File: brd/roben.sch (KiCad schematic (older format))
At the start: 92 parts, among them J1 POWER IN, J10 GND, J11 A, J12 C, J13 B, J14 D, J2 BT HC-05, J3 1+, J4 1-, J5 2+, J6 2-, J7 +V, J8 GND, J9 +V, Q1 BUK7Y98, Q2 BC856, SW1 POWER ON, SW2 SW_PUSH, SW3 SW_PUSH, U1 Ardunano, U2 LM3488, U3 SN754410N, U4 LM2902N

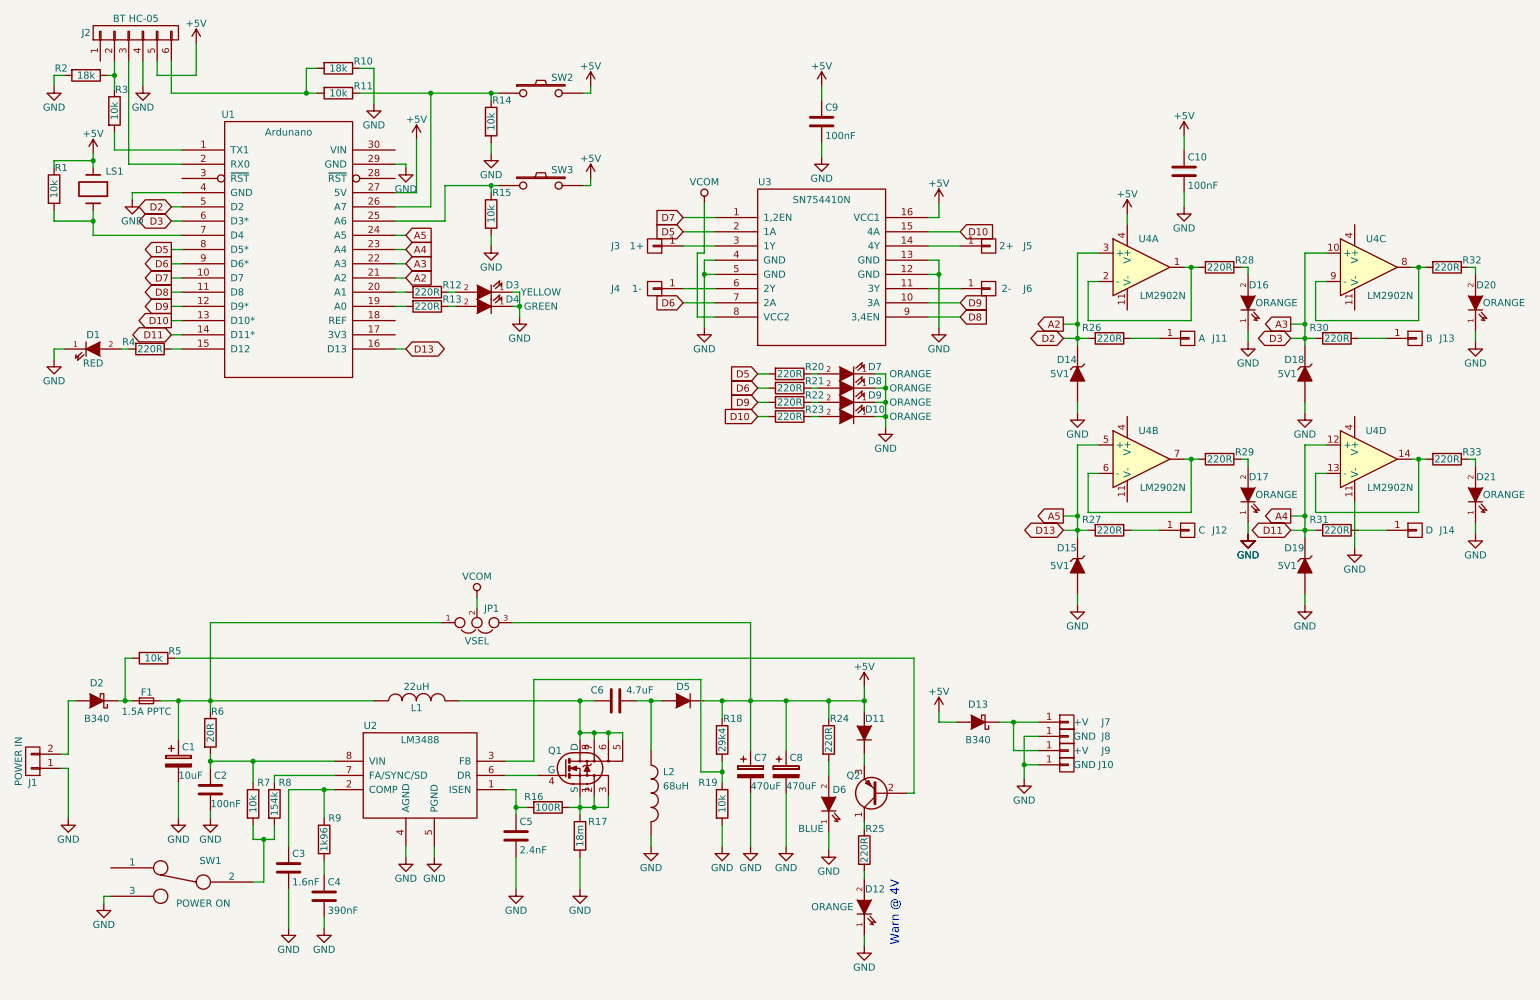
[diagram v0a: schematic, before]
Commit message: chg: creada netlist y asociaciones
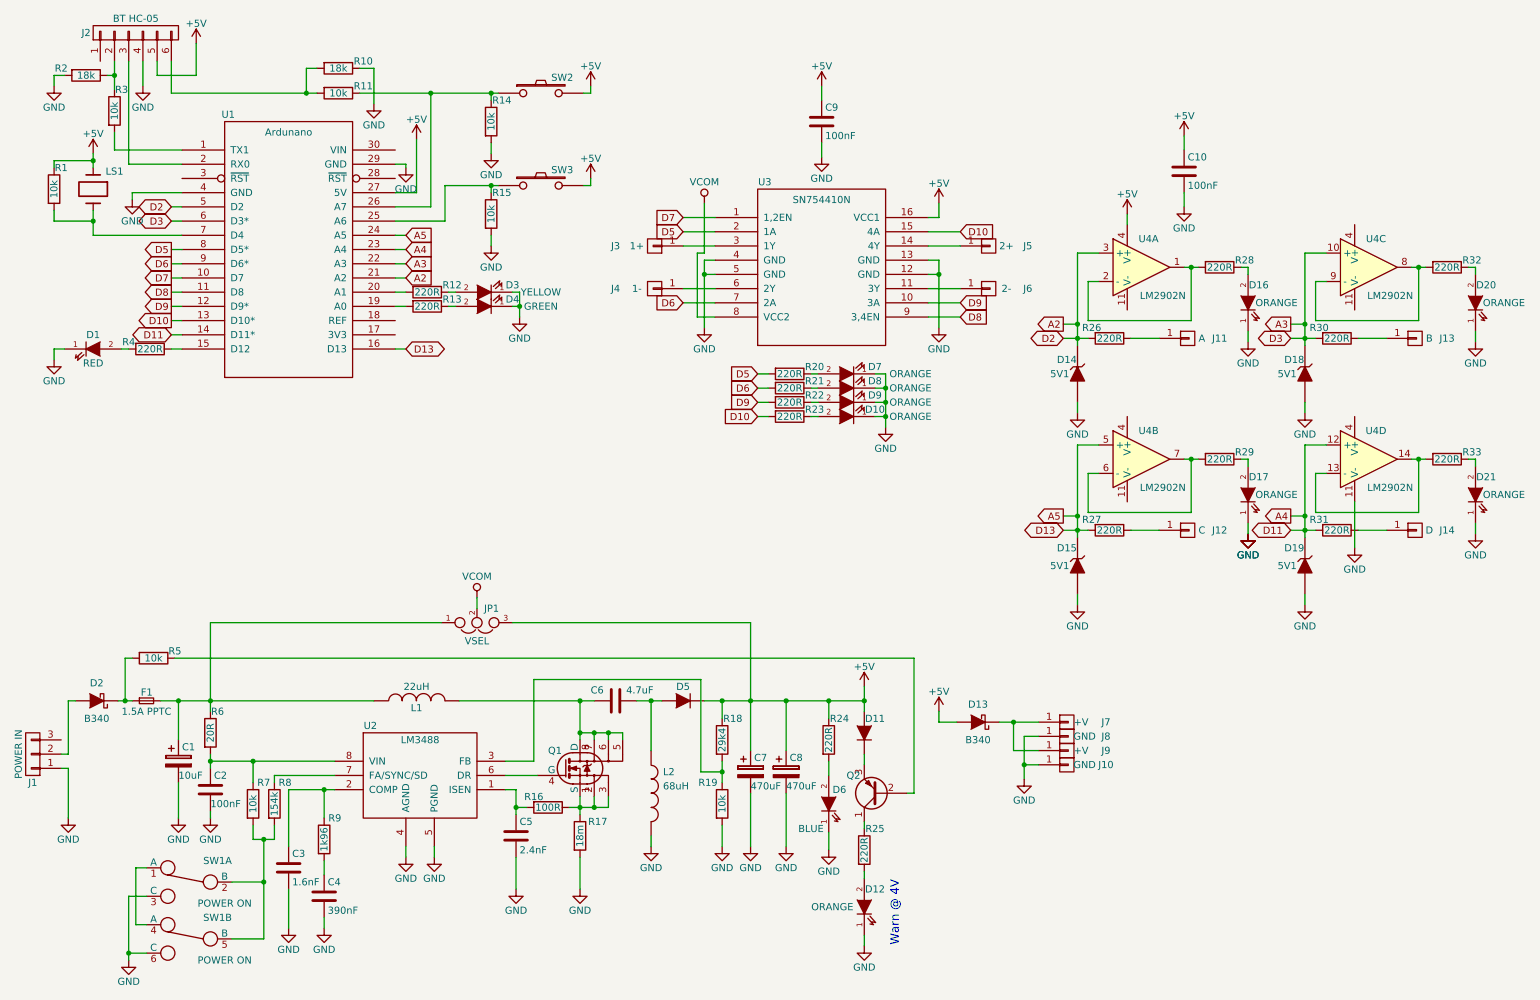
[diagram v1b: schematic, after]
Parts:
- removed J1: POWER IN, asrdi-conn:MKDSN-1985946-02, symbol CONN_01X02
- removed SW1: POWER ON, symbol SWITCH_INV
- added J1: POWER IN, symbol CONN_01X03
- added SW1: POWER ON, asrdi-switch:JS202011SCQN, symbol Switch_SPDT_x2
- C1: footprint (none) -> Capacitors_SMD:c_elec_5x5.3
- C2, C3, C4, C5: footprint (none) -> Capacitors_SMD:C_0805_HandSoldering
- C6: footprint (none) -> Capacitors_SMD:C_1206_HandSoldering
- C7, C8: footprint (none) -> Capacitors_SMD:c_elec_8x10
- D11: value D -> TCMBD914; footprint (none) -> Housings_SOT-23_SOT-143_TSOT-6:SOT-23_Handsoldering
- D5: footprint (none) -> Diodes_SMD:Diode-SMB_Handsoldering
- J2: footprint (none) -> Socket_Strips:Socket_Strip_Straight_1x06
- JP1: footprint (none) -> asrdi-conn:M20-87703xx
- L1: footprint (none) -> asrdi-discrete:coil-12x12h10
- L2: footprint (none) -> asrdi-discrete:coil-13x13H7
- LS1: footprint (none) -> asrdi-buzzer:AT-1224-TWT-5V-2-R
- Q1: footprint LFPAK56 -> Power_Packages_SMD:SOT-669_LFPAK_ThermalVias-1
- Q2: footprint (none) -> Housings_SOT-23_SOT-143_TSOT-6:SOT-23_Handsoldering
- R1, R10, R11, R14, R15, R16, R18, R19, R2, R25, R3, R5, R6, R7, R8, R9: footprint (none) -> Resistors_SMD:R_0805_HandSoldering
- R17: footprint (none) -> asrdi-discrete:0612
- SW2, SW3: footprint (none) -> asrdi-switch:FSMxxJxH
- U2: footprint MODULE -> Housings_SSOP:TSSOP-8_3x3mm_Pitch0.65mm
- U4: footprint (none) -> Housings_SOIC:SOIC-14_3.9x8.7mm_Pitch1.27mm
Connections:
- net GND: now also J1.1 (P1), SW1.3 (C), SW1.6 (C)
- net at D2.2 (A): now also J1.2 (P2)
- net at R7.2, R8.2: now also SW1.2 (B), SW1.5 (B)
- new net: SW1.1 (A), SW1.4 (A)

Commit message: chg: finalizado esquematico
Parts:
- J1: footprint (none) -> asrdi-conn:combo-barrel5.5x2.1-2p5.08; Vendor (none) -> 1776493-2 / RAPC722X
- SW1: Vendor (none) -> JS202011SCQN
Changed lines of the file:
@@
 F 2 "asrdi-switch:JS202011SCQN" H 1825 7000 50  0001 C CNN
 F 3 "" H 1825 7000 50  0000 C CNN
+F 4 "JS202011SCQN" H 1825 7000 60  0001 C CNN "Vendor"
 	1    1825 7000
 	-1   0    0    -1
@@
 F 2 "asrdi-switch:JS202011SCQN" H 1825 7400 50  0001 C CNN
 F 3 "" H 1825 7400 50  0000 C CNN
+F 4 "JS202011SCQN" H 1825 7400 60  0001 C CNN "Vendor"
 	2    1825 7400
 	-1   0    0    -1
@@
 F 0 "J1" H 725 6300 50  0000 C CNN
 F 1 "POWER IN" V 825 6100 50  0000 C CNN
-F 2 "" H 725 6100 50  0000 C CNN
+F 2 "asrdi-conn:combo-barrel5.5x2.1-2p5.08" H 725 6100 50  0001 C CNN
 F 3 "" H 725 6100 50  0000 C CNN
+F 4 "1776493-2 / RAPC722X" H 725 6100 60  0001 C CNN "Vendor"
 	1    725  6100
 	-1   0    0    1

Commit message: chg: corregida conexion bluetooth
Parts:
- removed D11: TCMBD914, Housings_SOT-23_SOT-143_TSOT-6:SOT-23_Handsoldering, symbol D
- removed R10: 18k, Resistors_SMD:R_0805_HandSoldering, symbol R
- removed R11: 10k, Resistors_SMD:R_0805_HandSoldering, symbol R
- added D11: TCMBD914, Housings_SOT-23_SOT-143_TSOT-6:SOT-23_Handsoldering, symbol Diode-sot23
- J2: footprint Socket_Strips:Socket_Strip_Straight_1x06 -> asrdi-socket:HC-05
- U1: footprint Housings_DIP:DIP-32__600_ELL -> asrdi-socket:Ardunano
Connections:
- net +5V: now also D11.1 (A)
- net A2: now also U4.5 (+); no longer U4.3 (+)
- net A5: now also U4.3 (+); no longer U4.5 (+)
- net at Q2.3 (E): now also D11.3 (K)
- new net: R28.2, U4.6 (-), U4.7
- new net: R29.2, U4.1, U4.2 (-)
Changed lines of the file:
@@
 LIBS:LM3488
 LIBS:fds8449
+LIBS:diode-sot23
 LIBS:roben-cache
 EELAYER 25 0
@@
 F 0 "U1" H 2100 3500 50  0000 C CNN
 F 1 "Ardunano" H 2525 3375 50  0000 C CNN
-F 2 "Housings_DIP:DIP-32__600_ELL" H 2525 2550 50  0001 C CNN
+F 2 "asrdi-socket:Ardunano" H 2525 2550 50  0001 C CNN
 F 3 "DOCUMENTATION" H 2525 2550 50  0001 C CNN
 F 4 "A000005 / 1-2199300-2" H 2525 2550 60  0001 C CNN "Vendor"
@@
 $Comp
 L LM2902N U4
-U 1 1 569DF9C0
+U 2 1 569DF9C0
 P 8525 2675
 F 0 "U4" H 8575 2875 50  0000 C CNN
@@
 F 3 "" H 8575 2875 50  0000 C CNN
 F 4 "LM2902DT" H 8525 2675 60  0001 C CNN "Vendor"
-	1    8525 2675
+	2    8525 2675
 	1    0    0    -1
 $EndComp
@@
 Warn @ 4V
 $Comp
-L D D11
-U 1 1 56A11248
-P 6575 5950
-F 0 "D11" V 6675 5875 50  0000 C CNN
-F 1 "TCMBD914" H 6575 5850 50  0001 C CNN
-F 2 "Housings_SOT-23_SOT-143_TSOT-6:SOT-23_Handsoldering" H 6575 5950 50  0001 C CNN
-F 3 "" H 6575 5950 50  0000 C CNN
-F 4 "TCMBD914" H 6575 5950 60  0001 C CNN "Vendor"
-	1    6575 5950
-	0    -1   -1   0
-$EndComp
-$Comp
 L GND #PWR029
 U 1 1 56A34D88
@@
 	1350 3250 1400 3250
 Wire Wire Line
-	3950 1450 3950 1500
-Wire Wire Line
 	4650 1400 4650 1450
 Wire Wire Line
@@
 	4650 2100 4600 2100
 Connection ~ 3950 2100
-Connection ~ 3950 1450
 Wire Wire Line
 	2275 6300 2275 6150
@@
 $Comp
 L LM2902N U4
-U 2 1 56A5BD0D
+U 1 1 56A5BD0D
 P 8525 4025
 F 0 "U4" H 8575 4225 50  0000 C CNN
@@
 F 3 "" H 8575 4225 50  0000 C CNN
 F 4 "LM2902DT" H 8525 4025 60  0001 C CNN "Vendor"
-	2    8525 4025
+	1    8525 4025
 	1    0    0    -1
 $EndComp
@@
 F 0 "J2" V 1450 1375 50  0000 C CNN
 F 1 "BT HC-05" V 1550 1025 50  0000 C CNN
-F 2 "Socket_Strips:Socket_Strip_Straight_1x06" H 1450 1025 50  0001 C CNN
+F 2 "asrdi-socket:HC-05" H 1450 1025 50  0001 C CNN
 F 3 "" H 1450 1025 50  0000 C CNN
 F 4 "61303211821" V 1450 1025 60  0001 C CNN "Vendor"
@@
 Wire Wire Line
 	1400 1950 1400 1225
-Connection ~ 3525 1450
 $Comp
 L +5V #PWR049
@@
 	875  1325 950  1325
 $Comp
-L R R11
-U 1 1 56A6FB3F
-P 2875 1450
-F 0 "R11" V 2825 1625 50  0000 C CNN
-F 1 "10k" V 2875 1450 50  0000 C CNN
-F 2 "Resistors_SMD:R_0805_HandSoldering" V 2805 1450 50  0001 C CNN
-F 3 "" H 2875 1450 50  0000 C CNN
-F 4 "ERJ-6ENF1002V" V 2875 1450 60  0001 C CNN "Vendor"
-	1    2875 1450
-	0    1    1    0
-$EndComp
-$Comp
-L R R10
-U 1 1 56A6FF7E
-P 2875 1275
-F 0 "R10" V 2825 1450 50  0000 C CNN
-F 1 "18k" V 2875 1275 50  0000 C CNN
-F 2 "Resistors_SMD:R_0805_HandSoldering" V 2805 1275 50  0001 C CNN
-F 3 "" H 2875 1275 50  0000 C CNN
-F 4 "ERJ-6ENF1802V" V 2875 1275 60  0001 C CNN "Vendor"
-	1    2875 1275
-	0    1    1    0
-$EndComp
-$Comp
-L GND #PWR052
-U 1 1 56A7014A
-P 3125 1525
-F 0 "#PWR052" H 3125 1275 50  0001 C CNN
-F 1 "GND" H 3125 1375 50  0000 C CNN
-F 2 "" H 3125 1525 60  0000 C CNN
-F 3 "" H 3125 1525 60  0000 C CNN
-	1    3125 1525
-	1    0    0    -1
-$EndComp
-Wire Wire Line
-	1700 1225 1700 1450
-Wire Wire Line
-	1700 1450 2725 1450
-Wire Wire Line
-	3025 1450 4000 1450
-Wire Wire Line
-	3125 1525 3125 1275
-Wire Wire Line
-	3125 1275 3025 1275
-Wire Wire Line
-	2725 1275 2650 1275
-Wire Wire Line
-	2650 1275 2650 1450
-Connection ~ 2650 1450
-$Comp
 L D_Schottky D2
 U 1 1 56A8478E
@@
 $EndComp
 $Comp
-L +5V #PWR053
+L +5V #PWR052
 U 1 1 56A8AB66
 P 8825 1750
-F 0 "#PWR053" H 8825 1600 50  0001 C CNN
+F 0 "#PWR052" H 8825 1600 50  0001 C CNN
 F 1 "+5V" H 8825 1890 50  0000 C CNN
 F 2 "" H 8825 1750 60  0000 C CNN
@@
 $EndComp
 $Comp
-L GND #PWR054
+L GND #PWR053
 U 1 1 56A8AB6C
 P 8825 2250
-F 0 "#PWR054" H 8825 2000 50  0001 C CNN
+F 0 "#PWR053" H 8825 2000 50  0001 C CNN
 F 1 "GND" H 8825 2100 50  0000 C CNN
 F 2 "" H 8825 2250 60  0000 C CNN
@@
 	-1   0    0    1
 $EndComp
+$Comp
+L Diode-sot23 D11
+U 1 1 56AC1C5C
+P 6575 5950
+F 0 "D11" V 6675 5875 50  0000 C CNN
+F 1 "TCMBD914" H 6575 5850 50  0001 C CNN
+F 2 "Housings_SOT-23_SOT-143_TSOT-6:SOT-23_Handsoldering" H 6575 5950 50  0001 C CNN
+F 3 "" H 6575 5950 50  0000 C CNN
+F 4 "TCMBD914" H 6575 5950 60  0001 C CNN "Vendor"
+	1    6575 5950
+	0    -1   -1   0
+$EndComp
+Wire Wire Line
+	3525 1450 4000 1450
+Wire Wire Line
+	3950 1500 3950 1450
+Connection ~ 3950 1450
 $EndSCHEMATC

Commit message: chg: reanotados componentes
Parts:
- renumbered R12 to R10, R13 to R11, R14 to R12, R15 to R13, R16 to R14, R17 to R15, R18 to R16, R19 to R17, R20 to R18, R21 to R19, R22 to R20, R23 to R21, R24 to R22, R25 to R23, R26 to R24, R27 to R25, R28 to R26, R29 to R27, R30 to R28, R31 to R29, R32 to R30, R33 to R31
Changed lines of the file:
@@
 $EndComp
 $Comp
-L R R26
+L R R24
 U 1 1 55BC0C32
 P 8300 3175
-F 0 "R26" V 8225 3050 50  0000 C CNN
+F 0 "R24" V 8225 3050 50  0000 C CNN
 F 1 "220R" V 8300 3175 50  0000 C CNN
 F 2 "Resistors_SMD:R_0805_HandSoldering" V 8230 3175 30  0001 C CNN
@@
 $EndComp
 $Comp
-L R R24
+L R R22
 U 1 1 55BD4565
 P 6325 6000
-F 0 "R24" H 6400 6150 50  0000 C CNN
+F 0 "R22" H 6400 6150 50  0000 C CNN
 F 1 "220R" V 6325 6000 50  0000 C CNN
 F 2 "Resistors_SMD:R_0805_HandSoldering" V 6255 6000 30  0001 C CNN
@@
 $EndComp
 $Comp
-L R R18
+L R R16
 U 1 1 569C49AB
 P 5575 6000
-F 0 "R18" H 5650 6150 50  0000 C CNN
+F 0 "R16" H 5650 6150 50  0000 C CNN
 F 1 "29k4" V 5575 6000 50  0000 C CNN
 F 2 "Resistors_SMD:R_0805_HandSoldering" V 5505 6000 50  0001 C CNN
@@
 $EndComp
 $Comp
-L R R19
+L R R17
 U 1 1 569C4A32
 P 5575 6450
-F 0 "R19" H 5475 6600 50  0000 C CNN
+F 0 "R17" H 5475 6600 50  0000 C CNN
 F 1 "10k" V 5575 6450 50  0000 C CNN
 F 2 "Resistors_SMD:R_0805_HandSoldering" V 5505 6450 50  0001 C CNN
@@
 $EndComp
 $Comp
-L R R17
+L R R15
 U 1 1 569D5A50
 P 4575 6675
-F 0 "R17" H 4700 6775 50  0000 C CNN
+F 0 "R15" H 4700 6775 50  0000 C CNN
 F 1 "18m" V 4575 6675 50  0000 C CNN
 F 2 "asrdi-discrete:0612" V 4505 6675 50  0001 C CNN
@@
 $EndComp
 $Comp
-L R R16
+L R R14
 U 1 1 569D5B05
 P 4350 6475
-F 0 "R16" V 4275 6375 50  0000 C CNN
+F 0 "R14" V 4275 6375 50  0000 C CNN
 F 1 "100R" V 4350 6475 50  0000 C CNN
 F 2 "Resistors_SMD:R_0805_HandSoldering" V 4280 6475 50  0001 C CNN
@@
 $EndComp
 $Comp
-L R R28
+L R R26
 U 1 1 569DF9C7
 P 9075 2675
-F 0 "R28" V 9025 2850 50  0000 C CNN
+F 0 "R26" V 9025 2850 50  0000 C CNN
 F 1 "220R" V 9075 2675 50  0000 C CNN
 F 2 "Resistors_SMD:R_0805_HandSoldering" V 9005 2675 30  0001 C CNN
@@
 $EndComp
 $Comp
-L R R12
+L R R10
 U 1 1 569E53E2
 P 3500 2850
-F 0 "R12" V 3450 3025 50  0000 C CNN
+F 0 "R10" V 3450 3025 50  0000 C CNN
 F 1 "220R" V 3500 2850 50  0000 C CNN
 F 2 "Resistors_SMD:R_0805_HandSoldering" V 3430 2850 30  0001 C CNN
@@
 $EndComp
 $Comp
-L R R13
+L R R11
 U 1 1 569E6466
 P 3500 2950
-F 0 "R13" V 3450 3125 50  0000 C CNN
+F 0 "R11" V 3450 3125 50  0000 C CNN
 F 1 "220R" V 3500 2950 50  0000 C CNN
 F 2 "Resistors_SMD:R_0805_HandSoldering" V 3430 2950 30  0001 C CNN
@@
 $EndComp
 $Comp
-L R R14
+L R R12
 U 1 1 569E85EC
 P 3950 1650
-F 0 "R14" H 4025 1800 50  0000 C CNN
+F 0 "R12" H 4025 1800 50  0000 C CNN
 F 1 "10k" V 3950 1650 50  0000 C CNN
 F 2 "Resistors_SMD:R_0805_HandSoldering" V 3880 1650 50  0001 C CNN
@@
 $EndComp
 $Comp
-L R R25
+L R R23
 U 1 1 569ED4B6
 P 6575 6775
-F 0 "R25" H 6650 6925 50  0000 C CNN
+F 0 "R23" H 6650 6925 50  0000 C CNN
 F 1 "220R" V 6575 6775 50  0000 C CNN
 F 2 "Resistors_SMD:R_0805_HandSoldering" V 6505 6775 50  0001 C CNN
@@
 $EndComp
 $Comp
-L R R15
+L R R13
 U 1 1 569E9F83
 P 3950 2300
-F 0 "R15" H 4025 2450 50  0000 C CNN
+F 0 "R13" H 4025 2450 50  0000 C CNN
 F 1 "10k" V 3950 2300 50  0000 C CNN
 F 2 "Resistors_SMD:R_0805_HandSoldering" V 3880 2300 50  0001 C CNN
@@
 Connection ~ 8075 3075
 $Comp
-L R R30
+L R R28
 U 1 1 56A58D48
 P 9900 3175
-F 0 "R30" V 9825 3050 50  0000 C CNN
+F 0 "R28" V 9825 3050 50  0000 C CNN
 F 1 "220R" V 9900 3175 50  0000 C CNN
 F 2 "Resistors_SMD:R_0805_HandSoldering" V 9830 3175 30  0001 C CNN
@@
 $EndComp
 $Comp
-L R R32
+L R R30
 U 1 1 56A58D68
 P 10675 2675
-F 0 "R32" V 10625 2850 50  0000 C CNN
+F 0 "R30" V 10625 2850 50  0000 C CNN
 F 1 "220R" V 10675 2675 50  0000 C CNN
 F 2 "Resistors_SMD:R_0805_HandSoldering" V 10605 2675 30  0001 C CNN
@@
 Connection ~ 9675 3075
 $Comp
-L R R27
+L R R25
 U 1 1 56A5BCF4
 P 8300 4525
-F 0 "R27" V 8225 4400 50  0000 C CNN
+F 0 "R25" V 8225 4400 50  0000 C CNN
 F 1 "220R" V 8300 4525 50  0000 C CNN
 F 2 "Resistors_SMD:R_0805_HandSoldering" V 8230 4525 30  0001 C CNN
@@
 $EndComp
 $Comp
-L R R29
+L R R27
 U 1 1 56A5BD14
 P 9075 4025
-F 0 "R29" V 9025 4200 50  0000 C CNN
+F 0 "R27" V 9025 4200 50  0000 C CNN
 F 1 "220R" V 9075 4025 50  0000 C CNN
 F 2 "Resistors_SMD:R_0805_HandSoldering" V 9005 4025 30  0001 C CNN
@@
 $EndComp
 $Comp
-L R R31
+L R R29
 U 1 1 56A5FA53
 P 9900 4525
-F 0 "R31" V 9825 4400 50  0000 C CNN
+F 0 "R29" V 9825 4400 50  0000 C CNN
 F 1 "220R" V 9900 4525 50  0000 C CNN
 F 2 "Resistors_SMD:R_0805_HandSoldering" V 9830 4525 30  0001 C CNN
@@
 $EndComp
 $Comp
-L R R33
+L R R31
 U 1 1 56A5FA73
 P 10675 4025
-F 0 "R33" V 10625 4200 50  0000 C CNN
+F 0 "R31" V 10625 4200 50  0000 C CNN
 F 1 "220R" V 10675 4025 50  0000 C CNN
 F 2 "Resistors_SMD:R_0805_HandSoldering" V 10605 4025 30  0001 C CNN
@@
 $EndComp
 $Comp
-L R R20
+L R R18
 U 1 1 56A6A551
 P 6050 3425
-F 0 "R20" V 6000 3600 50  0000 C CNN
+F 0 "R18" V 6000 3600 50  0000 C CNN
 F 1 "220R" V 6050 3425 50  0000 C CNN
 F 2 "Resistors_SMD:R_0805_HandSoldering" V 5980 3425 30  0001 C CNN
@@
 $EndComp
 $Comp
-L R R21
+L R R19
 U 1 1 56A6A558
 P 6050 3525
-F 0 "R21" V 6000 3700 50  0000 C CNN
+F 0 "R19" V 6000 3700 50  0000 C CNN
 F 1 "220R" V 6050 3525 50  0000 C CNN
 F 2 "Resistors_SMD:R_0805_HandSoldering" V 5980 3525 30  0001 C CNN
@@
 $EndComp
 $Comp
-L R R22
+L R R20
 U 1 1 56A6ADC3
 P 6050 3625
-F 0 "R22" V 6000 3800 50  0000 C CNN
+F 0 "R20" V 6000 3800 50  0000 C CNN
 F 1 "220R" V 6050 3625 50  0000 C CNN
 F 2 "Resistors_SMD:R_0805_HandSoldering" V 5980 3625 30  0001 C CNN
@@
 $EndComp
 $Comp
-L R R23
+L R R21
 U 1 1 56A6ADCA
 P 6050 3725
-F 0 "R23" V 6000 3900 50  0000 C CNN
+F 0 "R21" V 6000 3900 50  0000 C CNN
 F 1 "220R" V 6050 3725 50  0000 C CNN
 F 2 "Resistors_SMD:R_0805_HandSoldering" V 5980 3725 30  0001 C CNN
